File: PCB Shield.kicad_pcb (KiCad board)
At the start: 2 copper layers, 89 x 124 mm, 48 parts, among them J1 Conn_20to49, J10 TB002-500-02BE, J11 Conn_1to20, J12 TB002-500-02BE, J13 TB002-500-02BE, J14 TB002-500-02BE, J15 TB002-500-02BE, J16 TB002-500-02BE, J17 TB002-500-02BE, J18 TB002-500-02BE, J2 Conn_01x08_Socket, J3 Conn_20to49, J6 Conn_01x04_Socket, J7 Conn_01x04_Socket, J8 Conn_1to20, J9 OSTT7020150, Q1 IRLML2502TRPBF, SW1 C1353VQNAA, U2 74AHCT125S14-13, U3 ESDA6V1L

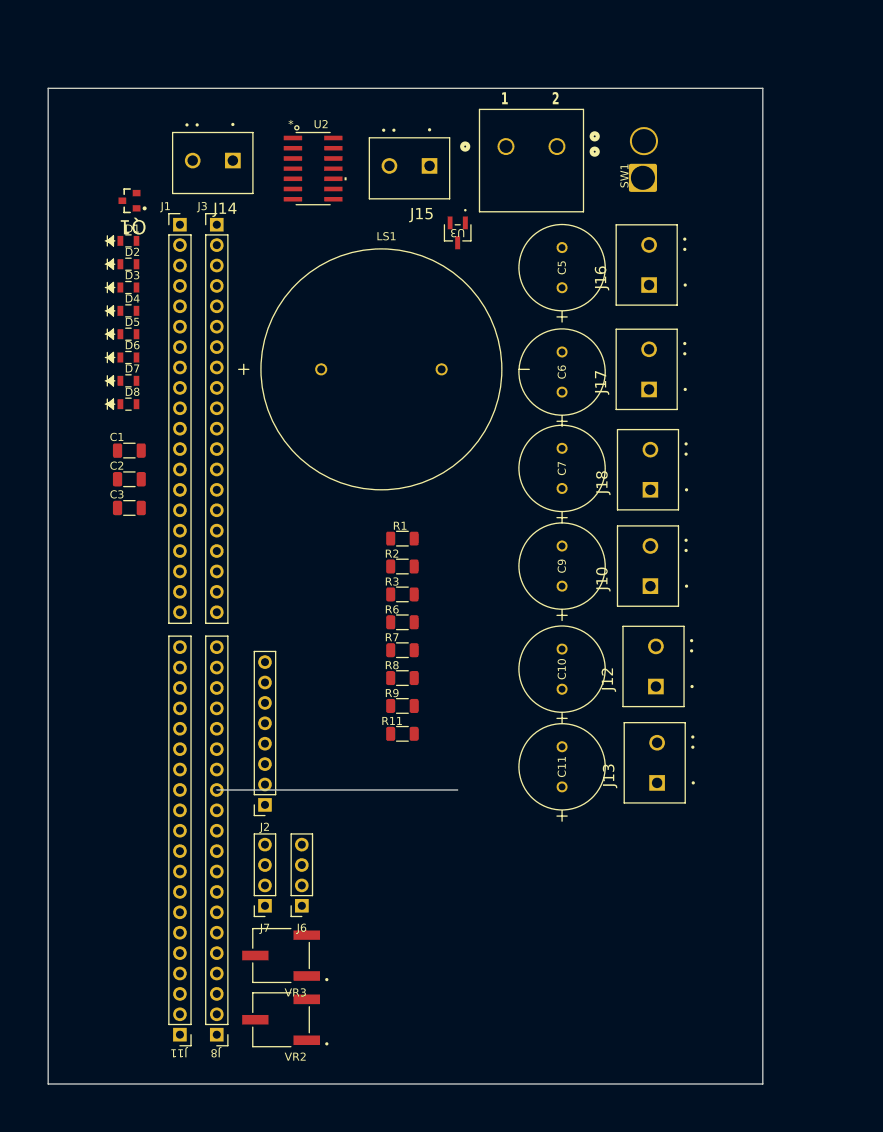
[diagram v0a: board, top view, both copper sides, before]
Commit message: placed PCB components somewhat how I want it
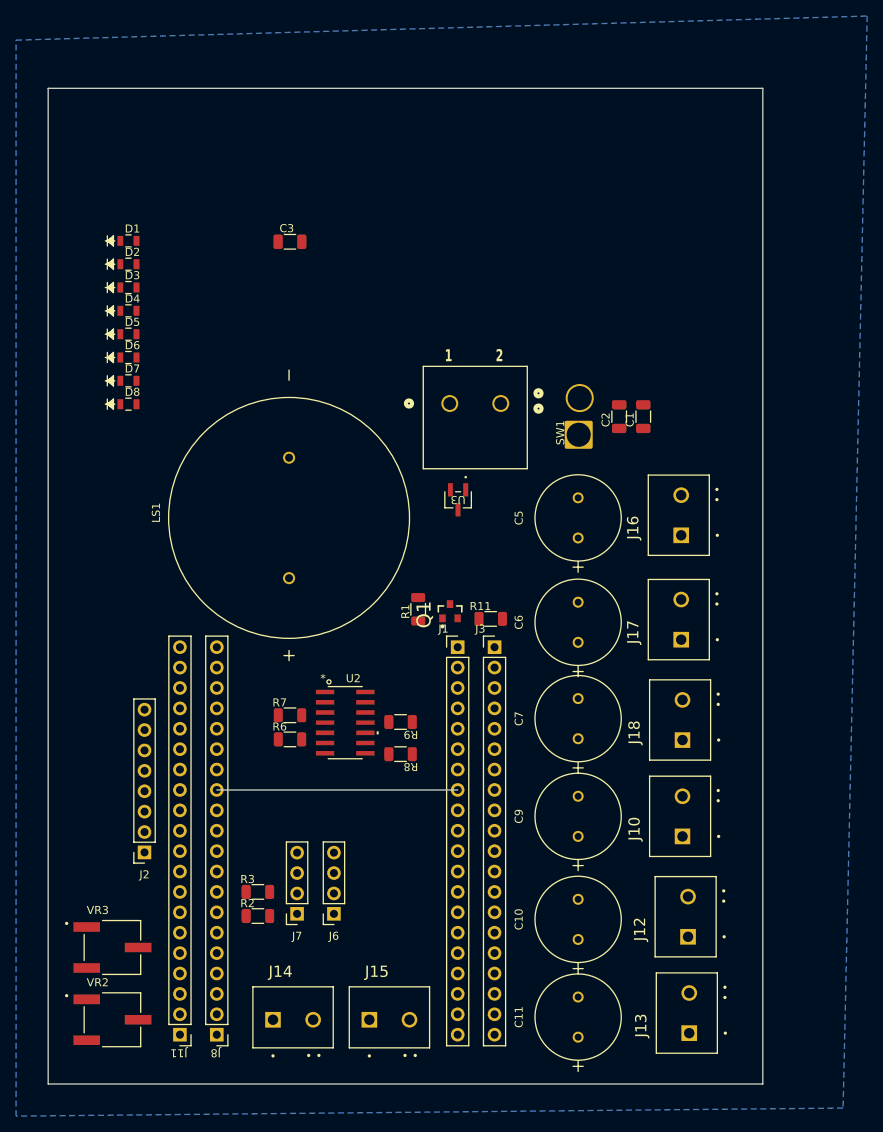
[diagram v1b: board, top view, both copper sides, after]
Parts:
- U2: value 74AHCT125S14-13 -> SO14_DIO
- moved J14 107.1 mm to (189.0, 150.0), turned to 0 degrees
- moved J15 106.6 mm to (201.0, 150.0), turned to 0 degrees
- moved U2 69.1 mm to (198.0, 113.0)
- moved C1 65.2 mm to (234.0, 77.2), turned to 90 degrees
- moved Q1 64.9 mm to (211.1, 99.1), turned to 90 degrees
- moved J1 63.0 mm to (210.2, 101.8)
- moved J3 63.0 mm to (214.8, 101.8)
- moved C2 62.3 mm to (231.0, 77.2), turned to 90 degrees
- moved R2 47.1 mm to (184.8, 136.0)
- moved R3 41.2 mm to (184.8, 133.0)
- moved C3 38.7 mm to (188.8, 52.0)
- moved U3 33.2 mm to (212.0, 85.2)
- moved SW1 33.0 mm to (225.3, 78.9)
- moved J9 32.8 mm to (211.0, 73.3)
- moved J12 31.4 mm to (240.7, 139.7)
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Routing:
- added copper zone on B.Cu, net GND

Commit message: routing almost done
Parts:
- U2: value SO14_DIO -> 74AHCT125S14-13
- moved C5 64.8 mm to (228.0, 154.8)
- moved C11 63.3 mm to (228.0, 88.8)
- moved J10 56.3 mm to (188.5, 149.8), turned to 0 degrees
- moved J14 56.1 mm to (240.8, 128.5), turned to 90 degrees
- moved C3 53.6 mm to (196.8, 105.0)
- moved C10 38.2 mm to (228.0, 101.8)
- moved C6 37.8 mm to (228.0, 140.8)
- moved J18 26.4 mm to (241.0, 88.8)
- moved J16 25.9 mm to (240.8, 115.5)
- moved D7 21.9 mm to (167.0, 92.0), turned to 90 degrees
- moved J12 15.8 mm to (240.8, 155.5)
- moved C7 13.0 mm to (228.0, 128.0)
- moved C9 12.4 mm to (228.0, 114.8)
- moved J13 10.2 mm to (240.8, 141.5)
- moved D8 3.80 mm to (168.0, 71.0), turned to 90 degrees
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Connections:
- C1 pad 1: Net-(J1-Pin_19) -> +5V
- C2 pad 1: Net-(J1-Pin_19) -> +5V
- J1 pad 5V: Net-(J1-Pin_19) -> +5V
- J3 pad 5V: Net-(J1-Pin_19) -> +5V
- SW1 pad 1: Net-(J1-Pin_19) -> +5V
- VR2 pad 1: 3V3 -> +3V3
- VR3 pad 1: 3V3 -> +3V3
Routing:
- net +5V: track 0.00 -> 200.2 mm
- net +3V3: track 0.00 -> 95.0 mm
- net SCLK: track 0.00 -> 18.2 mm
- net SCL / IO9: track 0.00 -> 16.5 mm
- net SDA / IO8: track 0.00 -> 14.1 mm
- net ADC1_3 / IO4: track 0.00 -> 12.4 mm
- net ADC1_0 / IO1: track 0.00 -> 10.7 mm
- net RST / IO15: track 0.00 -> 10.1 mm
- net MOSI / Data: track 0.00 -> 10.1 mm
- net MISO / Query: track 0.00 -> 9.00 mm
- net IRQ / IO14: track 0.00 -> 9.00 mm
- net CS / IO10: track 0.00 -> 9.00 mm
- net PWM / IO16: track 0.00 -> 4.59 mm
- net Net-(J11-Pin_9): track 0.00 -> 4.59 mm
- net Net-(J11-Pin_6): track 0.00 -> 4.59 mm
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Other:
- outline, holes or cut-outs redrawn
- board text removed: "Gabriel Haresco - Team 13"

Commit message: routing progress + planning
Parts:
- added R4: 0, Resistor_SMD:R_1206_3216Metric, F.Cu at (233.0, 72.0)
- moved D1 107.3 mm to (163.0, 160.0), turned to 180 degrees
- moved D2 106.0 mm to (191.0, 160.0)
- moved D3 76.4 mm to (247.0, 67.0)
- moved D4 34.4 mm to (205.0, 67.0)
- moved D5 26.6 mm to (197.0, 59.0)
- moved D6 26.6 mm to (197.0, 61.9)
- moved D7 21.4 mm to (163.0, 113.0), turned to 180 degrees
- moved J2 14.0 mm to (159.0, 129.0)
- moved C2 7.84 mm to (236.8, 69.0), turned to 0 degrees
- moved D8 6.40 mm to (163.0, 67.0), turned to 0 degrees
- moved C1 3.10 mm to (236.8, 73.0), turned to 0 degrees
- moved VR2 0.80 mm to (169.8, 150.0)
- moved VR3 0.80 mm to (169.8, 141.0)
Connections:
- C1 pad 1: +5V -> +5Vlimited
- C2 pad 1: +5V -> +5Vlimited
- J1 pad 5V: +5V -> +5Vlimited
- J3 pad 5V: +5V -> +5Vlimited
- J6 pad 3: +5V -> +5Vlimited
- J7 pad 3: +5V -> +5Vlimited
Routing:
- net SCLK: track 18.2 -> 4.59 mm
- net +5Vlimited: track 0.00 -> 12.6 mm
- net RST / IO15: track 10.1 -> 4.59 mm
- net MOSI / Data: track 10.1 -> 4.59 mm
- net +3V3: track 95.0 -> 90.1 mm
- net +5V: track 200.2 -> 195.7 mm
- net MISO / Query: track 9.00 -> 4.59 mm
- net IRQ / IO14: track 9.00 -> 4.59 mm
- net CS / IO10: track 9.00 -> 4.59 mm
- net ADC1_3 / IO4: track 12.4 -> 10.3 mm
- net ADC1_0 / IO1: track 10.7 -> 9.97 mm
- net GND: vias 0 -> 6
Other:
- board size 89 x 124 mm -> 93 x 98 mm

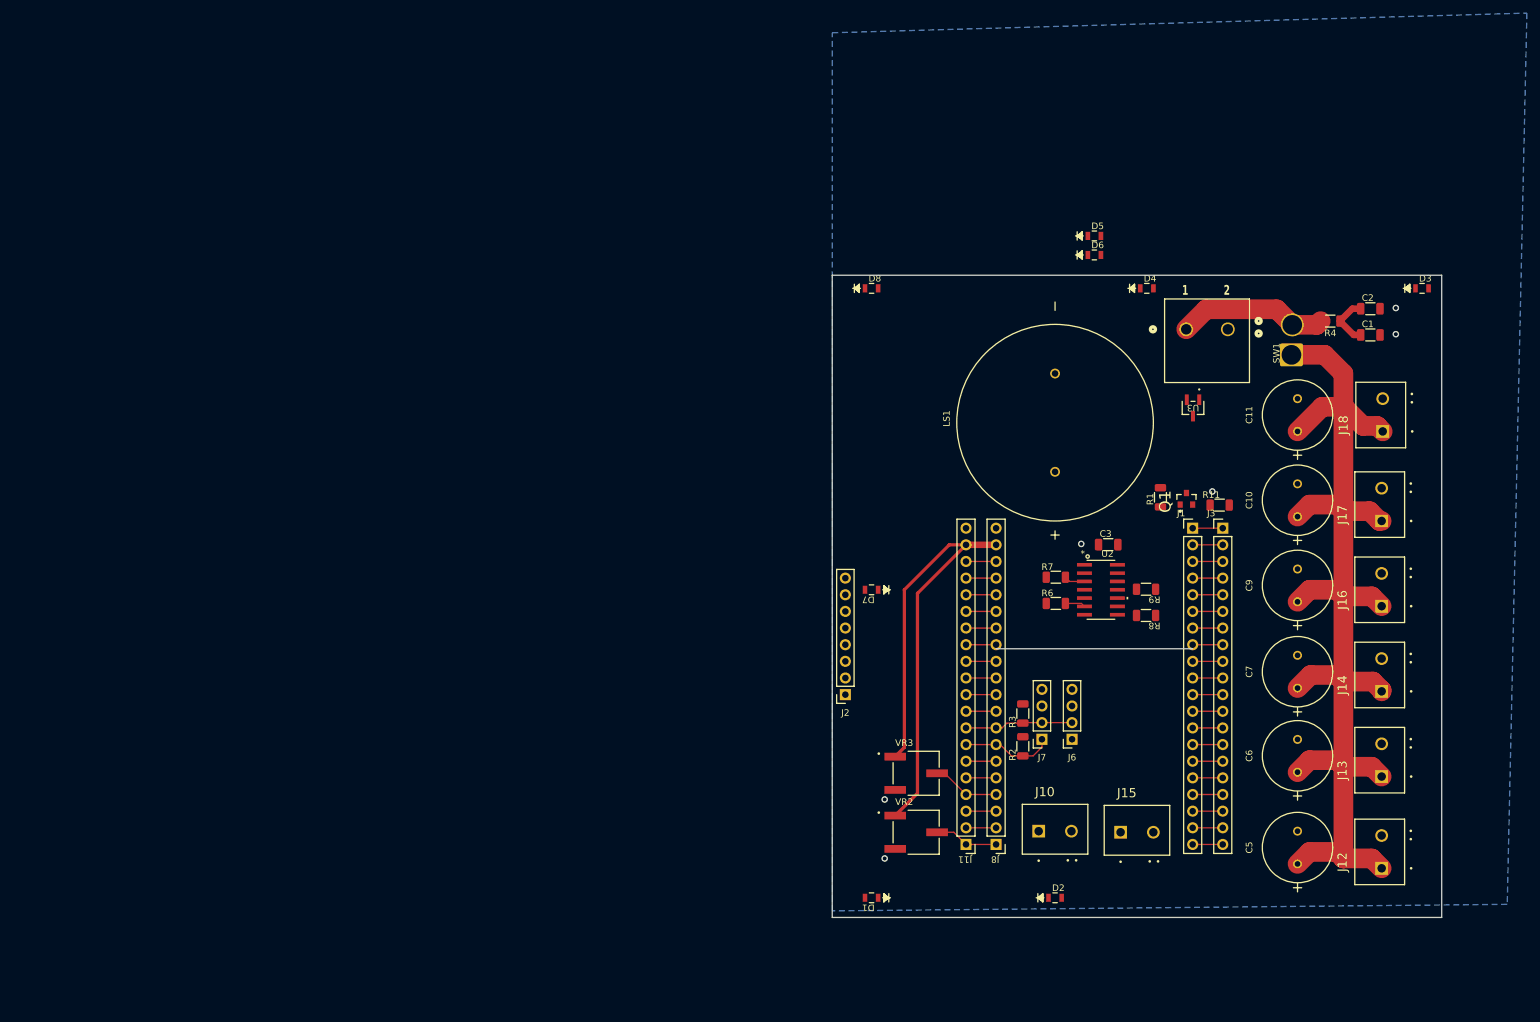
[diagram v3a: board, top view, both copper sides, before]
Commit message: most of routing finished
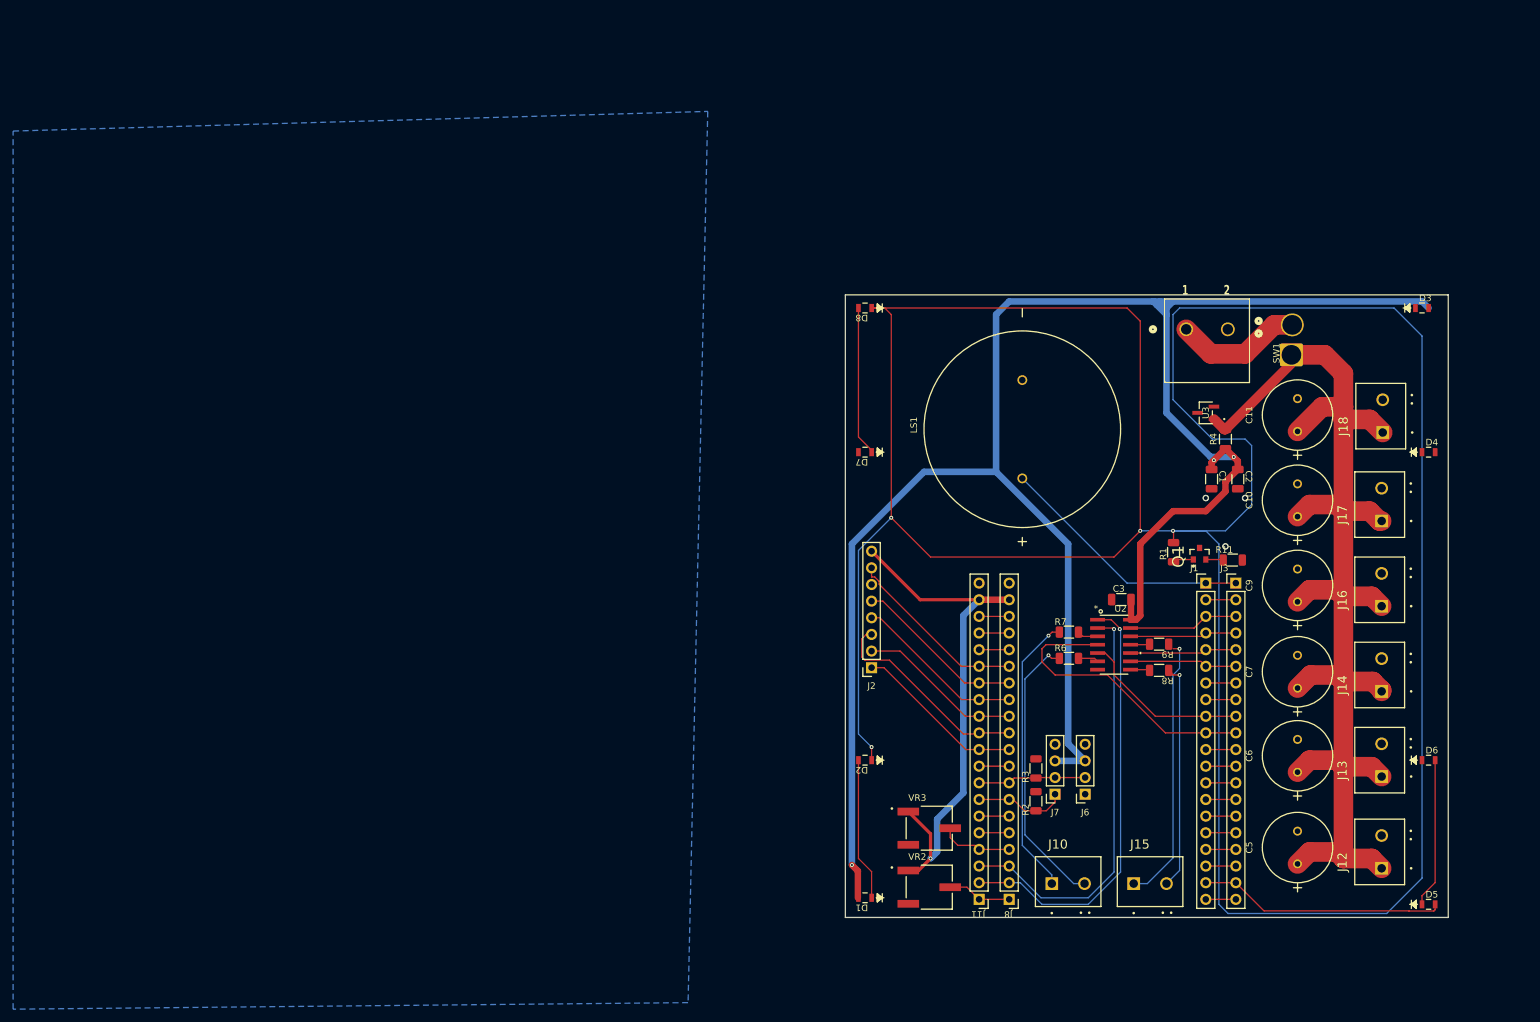
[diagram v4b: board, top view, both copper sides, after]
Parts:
- moved D5 114.0 mm to (248.0, 161.0)
- moved D6 92.4 mm to (248.0, 139.0)
- moved D4 49.7 mm to (248.0, 92.0)
- moved D2 35.8 mm to (162.0, 139.0), turned to 180 degrees
- moved C2 30.0 mm to (220.0, 93.8), turned to -90 degrees
- moved C1 29.4 mm to (216.0, 93.8), turned to -90 degrees
- moved R4 24.1 mm to (217.0, 90.0), turned to 90 degrees
- moved D7 21.0 mm to (162.0, 92.0)
- moved J11 8.62 mm to (181.2, 162.0)
- moved J8 8.62 mm to (185.8, 162.0)
- moved J1 8.62 mm to (212.2, 110.2)
- moved J3 8.62 mm to (216.8, 110.2)
- moved Q1 8.62 mm to (213.1, 107.5)
- moved R11 8.62 mm to (215.8, 107.4)
- moved R6 8.62 mm to (190.8, 122.4)
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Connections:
- C3 pad 2: +5V -> +5Vlimited
- D1 pad 2: +5V -> +5Vlimited
- D3 pad 2: +5V -> +5Vlimited
- D5 pad 2: +5V -> +5Vlimited
- D7 pad 2: +5V -> +5Vlimited
- U2 pad 14: +5V -> +5Vlimited
- U3 pad 2: +5V -> +5Vlimited
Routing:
- net LED split: track 0.00 -> 467.2 mm, vias 0 -> 4
- net +5Vlimited: track 12.6 -> 343.9 mm, vias 0 -> 3
- net EN1 / IO2: track 4.59 -> 66.2 mm, vias 0 -> 1
- net A1 / IO3: track 4.59 -> 63.9 mm, vias 0 -> 1
- net Net-(J10-Pad1): track 0.00 -> 43.2 mm, vias 0 -> 1
- net Net-(J10-Pad2): track 0.00 -> 42.9 mm, vias 0 -> 1
- net Net-(J15-Pad1): track 0.00 -> 40.9 mm, vias 0 -> 1
- net IO37: track 4.59 -> 44.8 mm
- net PWM / IO16: track 4.59 -> 39.2 mm
- net Net-(J15-Pad2): track 0.00 -> 34.6 mm, vias 0 -> 1
- net MOSI / Data: track 4.59 -> 32.0 mm
- net RST / IO15: track 4.59 -> 28.3 mm
- net Net-(D5-Pad1): track 0.00 -> 22.8 mm
- net Net-(D7-Pad1): track 0.00 -> 22.8 mm
- net Net-(D1-Pad1): track 0.00 -> 21.8 mm
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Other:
- board size 93 x 98 mm -> 92 x 95 mm

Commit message: finished routing and now just need to check 3d models
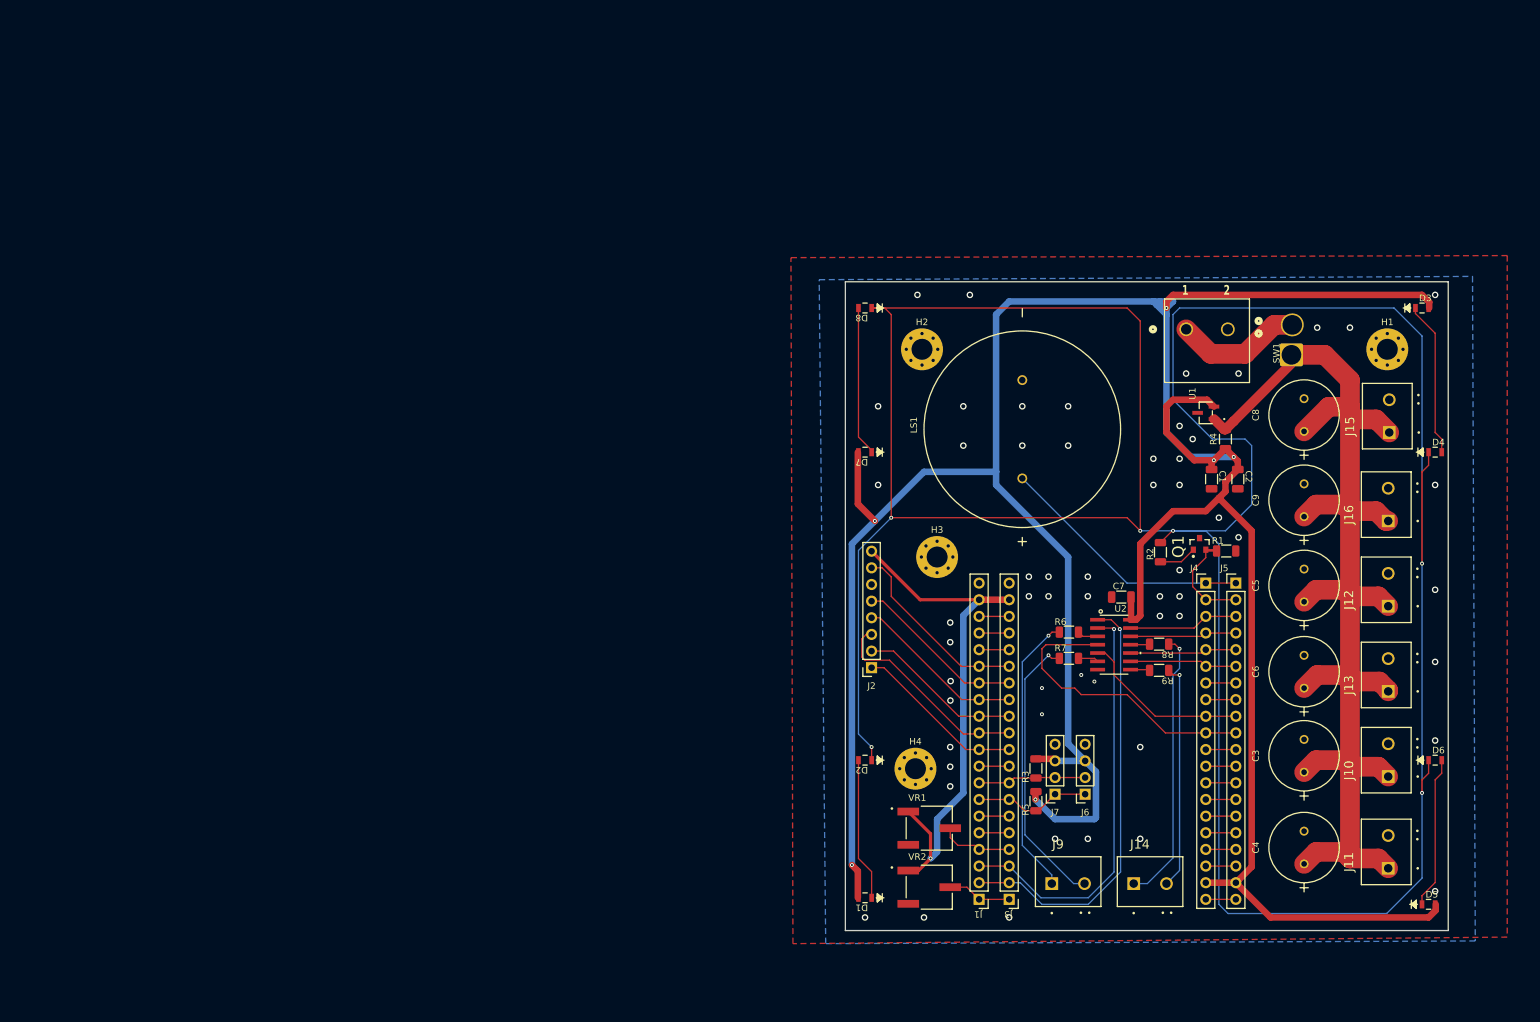
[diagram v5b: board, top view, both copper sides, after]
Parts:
- added H1: MountingHole, 196_Project_Footprints:MountingHole_3.2mm_M3_Pad_Via, F.Cu at (241.7, 76.3)
- added H2: MountingHole, 196_Project_Footprints:MountingHole_3.2mm_M3_Pad_Via, F.Cu at (170.7, 76.3)
- added H3: MountingHole, 196_Project_Footprints:MountingHole_3.2mm_M3_Pad_Via, F.Cu at (173.0, 108.0)
- added H4: MountingHole, 196_Project_Footprints:MountingHole_3.2mm_M3_Pad_Via, F.Cu at (169.7, 140.3)
- R4: value 0 -> R_Small_US
- U2: value 74AHCT125S14-13 -> SO14_DIO
- moved R2 2.00 mm to (206.0, 109.6)
- moved R1 1.70 mm to (214.8, 106.0)
- moved Q1 1.50 mm to (213.1, 106.0)
- moved D4 1.00 mm to (249.0, 92.0)
- moved D6 1.00 mm to (249.0, 139.0)
- moved C3 1.00 mm to (229.0, 140.8)
- moved C4 1.00 mm to (229.0, 154.8)
- moved C5 1.00 mm to (229.0, 114.8)
- moved C6 1.00 mm to (229.0, 128.0)
- moved C8 1.00 mm to (229.0, 88.8)
- moved C9 1.00 mm to (229.0, 101.8)
- moved J10 1.00 mm to (241.8, 141.5)
- moved J11 1.00 mm to (241.8, 155.5)
- moved J12 1.00 mm to (241.8, 115.5)
- moved J13 1.00 mm to (241.8, 128.5)
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- renumbered C6 to C3, C5 to C4, C9 to C5, C7 to C6, C3 to C7, C11 to C8, C10 to C9, J11 to J1, J13 to J10, J12 to J11, J16 to J12, J14 to J13, J15 to J14, J18 to J15, J17 to J16, J8 to J3, J1 to J4, J3 to J5, J9 to J8, J10 to J9, R11 to R1, R1 to R2, R2 to R5, R7 to R6, R6 to R7, R9 to R8, R8 to R9, U3 to U1, VR3 to VR1
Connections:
- R3 pad 2: +5V -> +5Vlimited
- R5 pad 2: +5V -> +5Vlimited
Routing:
- net +5Vlimited: track 343.9 -> 469.0 mm, vias 3 -> 6
- net Net-(D3-Pad1): track 0.00 -> 23.7 mm
- net LED split: track 467.2 -> 487.7 mm, vias 4 -> 6
- net GATE / IO45: track 7.28 -> 17.4 mm
- net SDA / IO8: track 14.1 -> 17.9 mm
- net Net-(Q1-D): track 3.16 -> 5.78 mm
- net Net-(J14-Pad1): track 40.9 -> 41.9 mm
- net RST / IO15: track 28.3 -> 29.0 mm
- net IO37: track 44.8 -> 45.4 mm
- net GND: vias 3 -> 57
- added copper zone on F.Cu, net GND
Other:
- board size 92 x 95 mm -> 92 x 99 mm
- board text added: "90mm"
- board text added: "99mm"
